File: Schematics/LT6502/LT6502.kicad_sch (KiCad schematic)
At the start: 37 parts, among them U1 TC1232, U2 W65C02S6TQG-14, U3 IS62C256AL, U4 IS62C256AL, U5 SST39SF010

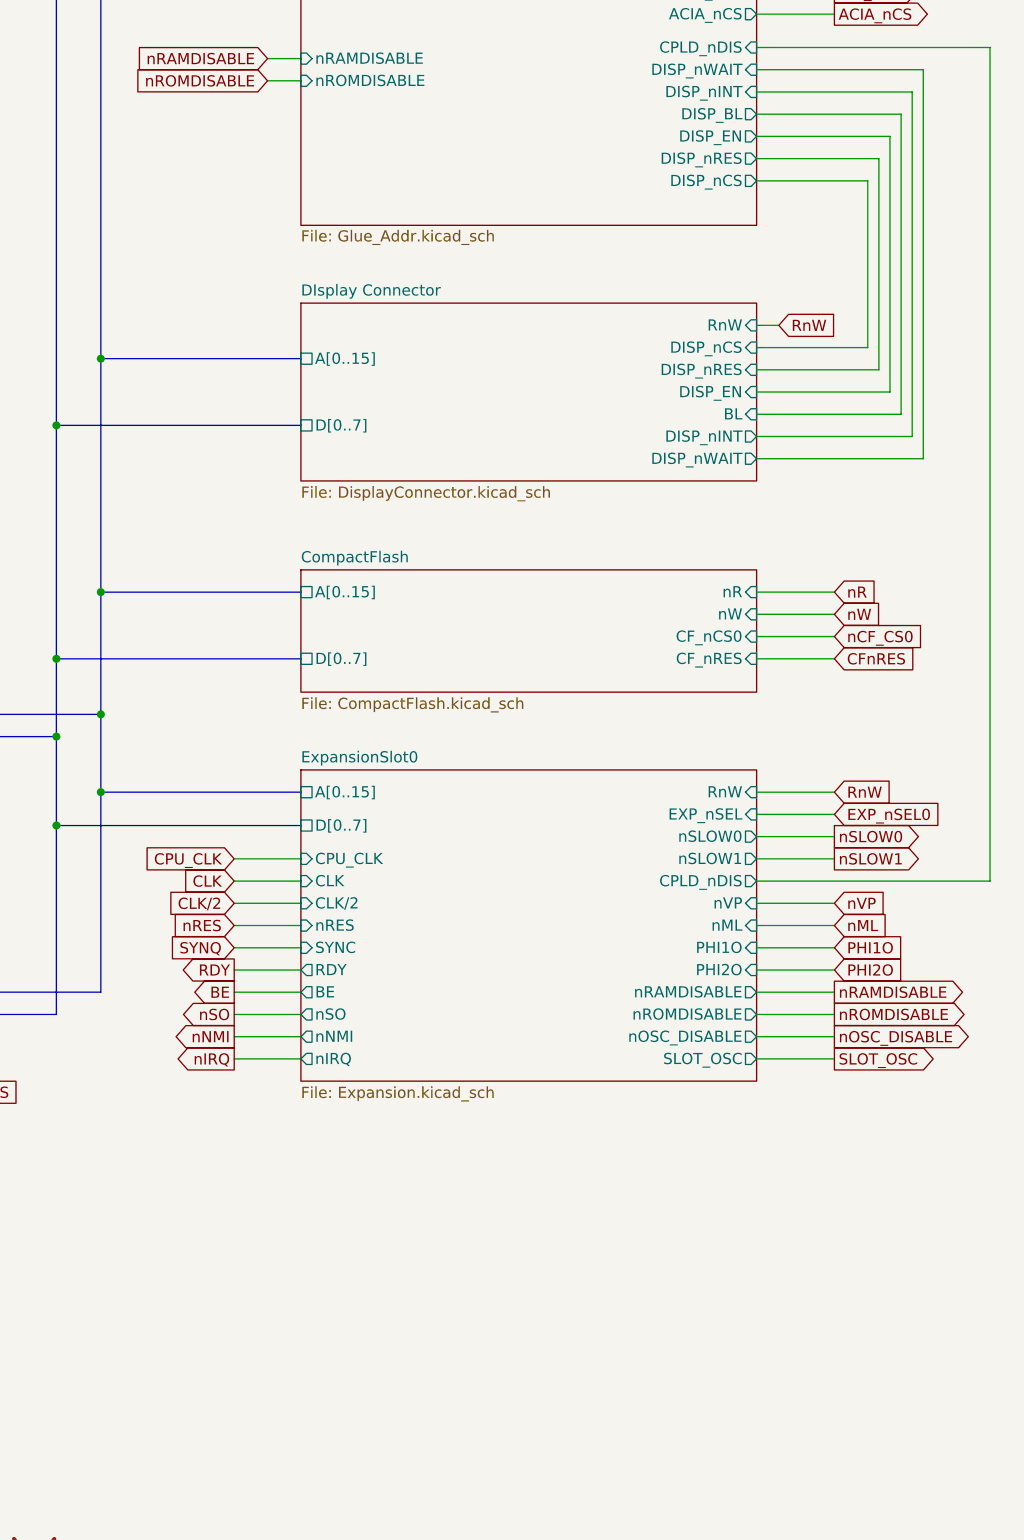
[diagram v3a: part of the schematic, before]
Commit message: Added speaker
Added a simple LM386/speaker and link to CPLD for simple audio.
Updated step files
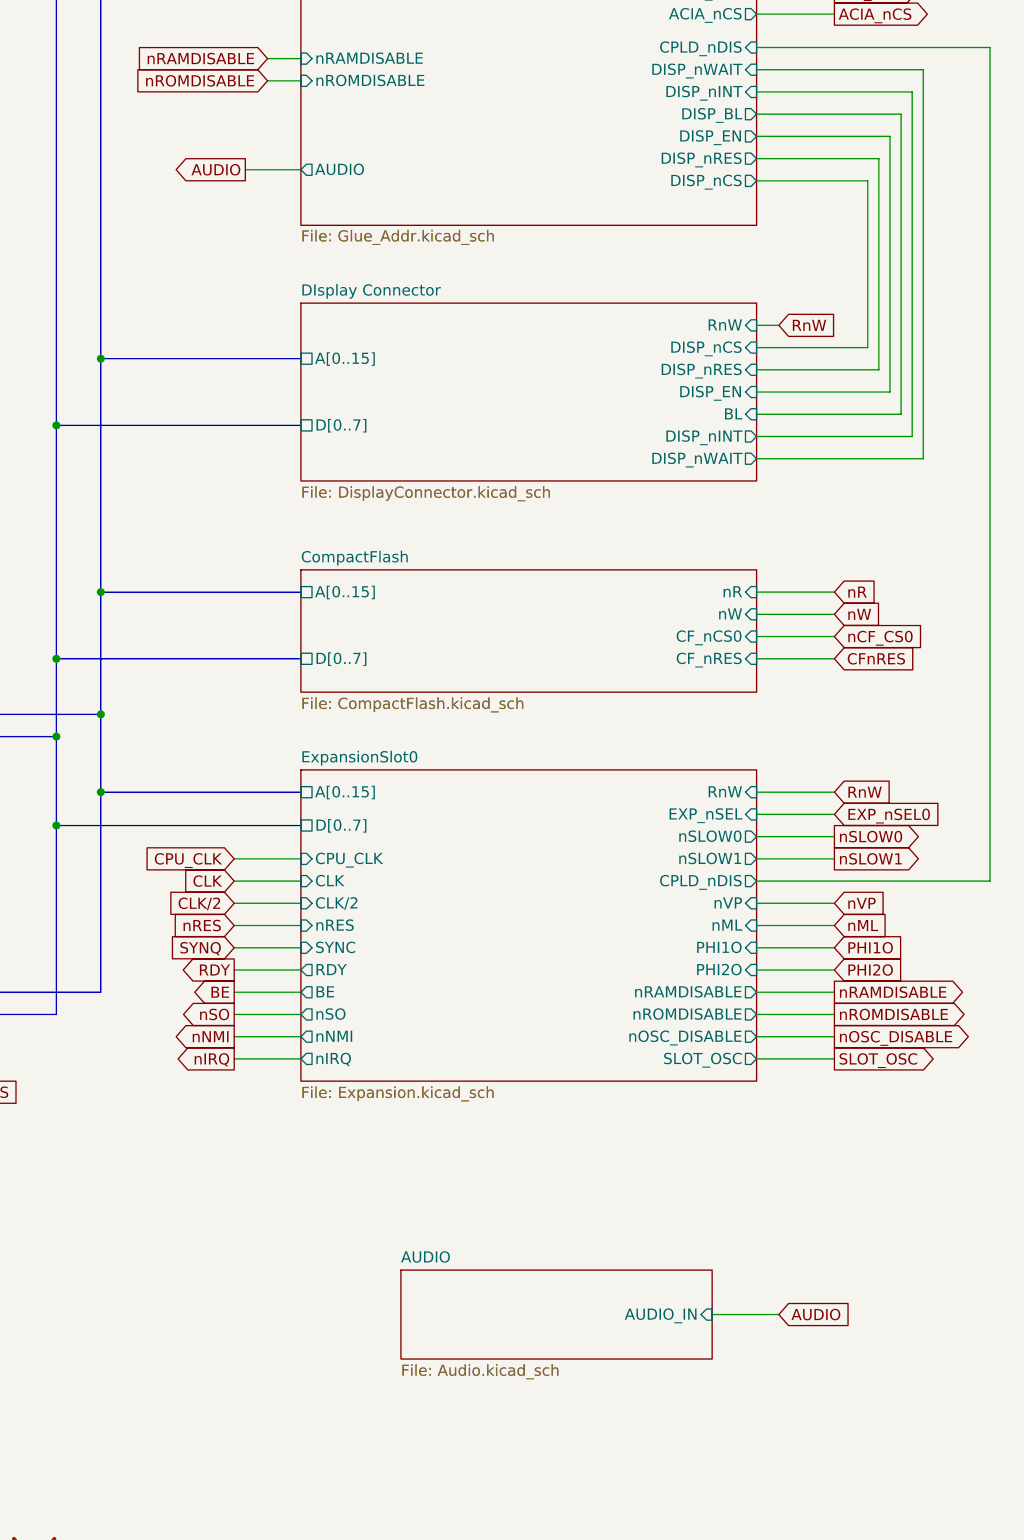
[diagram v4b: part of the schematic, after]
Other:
- added sheet AUDIO (Audio.kicad_sch)
- sheet Glue_Addr ports: added AUDIO; removed none
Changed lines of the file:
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@@
 	(wire
 		(pts
+			(xy 237.49 238.76) (xy 245.11 238.76)
+		)
+		(stroke
+			(width 0)
+			(type default)
+		)
+	)
+	(wire
+		(pts
 			(xy 92.71 44.45) (xy 92.71 41.91)
 		)
@@
 	(wire
 		(pts
+			(xy 184.15 107.95) (xy 190.5 107.95)
+		)
+		(stroke
+			(width 0)
+			(type default)
+		)
+	)
+	(wire
+		(pts
 			(xy 316.23 50.8) (xy 306.07 50.8)
 		)
@@
 		)
 	)
+	(global_label "AUDIO"
+		(shape output)
+		(at 184.15 107.95 180)
+		(fields_autoplaced yes)
+		(effects
+			(font
+				(size 1.27 1.27)
+			)
+			(justify right)
+		)
+		(property "Intersheetrefs" "${INTERSHEET_REFS}"
+			(at 175.5404 107.95 0)
+			(effects
+				(font
+					(size 1.27 1.27)
+				)
+				(justify right)
+				(hide yes)
+			)
+		)
+	)
 	(global_label "nSO"
 		(shape input)
@@
 		)
 	)
+	(global_label "AUDIO"
+		(shape input)
+		(at 245.11 238.76 0)
+		(fields_autoplaced yes)
+		(effects
+			(font
+				(size 1.27 1.27)
+			)
+			(justify left)
+		)
+		(property "Intersheetrefs" "${INTERSHEET_REFS}"
+			(at 253.7196 238.76 0)
+			(effects
+				(font
+					(size 1.27 1.27)
+				)
+				(justify left)
+				(hide yes)
+			)
+		)
+	)
 	(global_label "BE"
 		(shape input)
@@
 	)
 	(sheet
+		(at 201.93 233.68)
+		(size 35.56 10.16)
+		(exclude_from_sim no)
+		(in_bom yes)
+		(on_board yes)
+		(dnp no)
+		(fields_autoplaced yes)
+		(stroke
+			(width 0.1524)
+			(type solid)
+		)
+		(fill
+			(color 0 0 0 0.0000)
+		)
+		(property "Sheetname" "AUDIO"
+			(at 201.93 232.9684 0)
+			(effects
+				(font
+					(size 1.27 1.27)
+				)
+				(justify left bottom)
+			)
+		)
+		(property "Sheetfile" "Audio.kicad_sch"
+			(at 201.93 244.4246 0)
+			(effects
+				(font
+					(size 1.27 1.27)
+				)
+				(justify left top)
+			)
+		)
+		(pin "AUDIO_IN" input
+			(at 237.49 238.76 0)
+			(effects
+				(font
+					(size 1.27 1.27)
+				)
+				(justify right)
+			)
+		)
+		(instances
+			(project "LT6502"
+				(path "/a2243a34-697c-4939-97f7-df548e421864"
+					(page "10")
+				)
+			)
+		)
+	)
+	(sheet
 		(at 378.46 191.77)
 		(size 20.32 40.64)
@@
 			)
 		)
+		(pin "AUDIO" output
+			(at 190.5 107.95 180)
+			(effects
+				(font
+					(size 1.27 1.27)
+				)
+				(justify left)
+			)
+		)

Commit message: Updated BoMs ordered PCBs
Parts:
- C1, C2, C3, C4, C5, C53: LCSC C49678 -> C113803
- JP1, JP2, U1, U2, U3, U4: LCSC (none) -> DNF; now not fitted
- R1, R10, R7, R8: LCSC DNF -> C25890
- R9: LCSC C23179 -> C11702
- S2, U5: now not fitted
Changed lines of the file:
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@@
 			)
 		)
-		(property "LCSC" "DNF"
+		(property "LCSC" "C25890"
 			(at 33.02 162.56 0)
 			(effects
@@
 		(in_bom yes)
 		(on_board yes)
-		(dnp no)
+		(dnp yes)
 		(fields_autoplaced yes)
 		(property "Reference" "U3"
@@
 			)
 		)
+		(property "LCSC" "DNF"
+			(at 328.93 58.42 0)
+			(effects
+				(font
+					(size 1.27 1.27)
+				)
+				(hide yes)
+			)
+		)
 		(pin "7"
 		)
@@
 		(in_bom no)
 		(on_board yes)
-		(dnp no)
+		(dnp yes)
 		(fields_autoplaced yes)
 		(property "Reference" "JP1"
@@
 			)
 		)
+		(property "LCSC" "DNF"
+			(at 41.91 147.32 0)
+			(effects
+				(font
+					(size 1.27 1.27)
+				)
+				(hide yes)
+			)
+		)
 		(pin "3"
 		)
@@
 		(in_bom yes)
 		(on_board yes)
-		(dnp no)
+		(dnp yes)
 		(fields_autoplaced yes)
 		(property "Reference" "U2"
@@
 			)
 		)
+		(property "LCSC" "DNF"
+			(at 121.92 90.17 0)
+			(effects
+				(font
+					(size 1.27 1.27)
+				)
+				(hide yes)
+			)
+		)
 		(pin "2"
 		)
@@
 			)
 		)
-		(property "LCSC" "C23179"
+		(property "LCSC" "C11702"
 			(at 77.47 194.31 90)
 			(effects
@@
 			)
 		)
-		(property "LCSC" "C49678"
+		(property "LCSC" "C113803"
 			(at 54.61 265.43 0)
 			(effects
@@
 			)
 		)
-		(property "LCSC" "DNF"
+		(property "LCSC" "C25890"
 			(at 92.71 38.1 0)
 			(effects
@@
 			)
 		)
-		(property "LCSC" "C49678"
+		(property "LCSC" "C113803"
 			(at 31.75 265.43 0)
 			(effects
@@
 			)
 		)
-		(property "LCSC" "C49678"
+		(property "LCSC" "C113803"
 			(at 88.9 265.43 0)
 			(effects
@@
 		(in_bom no)
 		(on_board yes)
-		(dnp no)
+		(dnp yes)
 		(property "Reference" "JP2"
 			(at 60.96 134.62 0)
@@
 			)
 		)
+		(property "LCSC" "DNF"
+			(at 60.96 140.97 0)
+			(effects
+				(font
+					(size 1.27 1.27)
+				)
+				(hide yes)
+			)
+		)
 		(pin "3"
 		)
@@
 			)
 		)
-		(property "LCSC" "C49678"
+		(property "LCSC" "C113803"
 			(at 25.4 265.43 0)
 			(effects
@@
 		(in_bom yes)
 		(on_board yes)
-		(dnp no)
+		(dnp yes)
 		(fields_autoplaced yes)
 		(property "Reference" "U4"
@@
 			)
 		)
+		(property "LCSC" "DNF"
+			(at 328.93 119.38 0)
+			(effects
+				(font
+					(size 1.27 1.27)
+				)
+				(hide yes)
+			)
+		)
 		(pin "7"
 		)
@@
 		(in_bom yes)
 		(on_board yes)
-		(dnp no)
+		(dnp yes)
 		(property "Reference" "S2"
 			(at 27.178 183.134 0)
@@
 		(in_bom yes)
 		(on_board yes)
-		(dnp no)
+		(dnp yes)
 		(property "Reference" "U5"
 			(at 337.185 158.75 0)
@@
 			)
 		)
-		(property "LCSC" "DNF"
+		(property "LCSC" "C25890"
 			(at 83.82 38.1 0)
 			(effects
@@
 			)
 		)
-		(property "LCSC" "C49678"
+		(property "LCSC" "C113803"
 			(at 60.96 265.43 0)
 			(effects
@@
 		(in_bom yes)
 		(on_board yes)
-		(dnp no)
+		(dnp yes)
 		(fields_autoplaced yes)
 		(property "Reference" "U1"
@@
 			)
 		)
+		(property "LCSC" "DNF"
+			(at 74.93 167.64 0)
+			(effects
+				(font
+					(size 1.27 1.27)
+				)
+				(hide yes)
+			)
+		)
 		(pin "2"
 		)
@@
 			)
 		)
-		(property "LCSC" "DNF"
+		(property "LCSC" "C25890"
 			(at 99.06 160.02 0)
 			(effects
@@
 			)
 		)
-		(property "LCSC" "C49678"
+		(property "LCSC" "C113803"
 			(at 82.55 265.43 0)
 			(effects

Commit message: Auto stash before merge of "main" and "origin/main"
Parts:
- added TP7: TestPoint, TestPoint:TestPoint_Loop_D1.80mm_Drill1.0mm_Beaded, symbol Connector:TestPoint
- S2, U1, U2, U3, U4, U5: now fitted
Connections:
- net at R1.2, S2.1, S2.2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: now also TP7.1
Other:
- sheet DIsplay Connector renamed Display Connector
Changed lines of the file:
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@@
 		)
 	)
+	(text_box "V1.0-V1.1 Changes\nAdded cutout for reset switch\nAdded cutout for LS1 and moved it\nExpanded pads on L2 for ease of soldering\nChange R46 to 51K\nChange R47 to 120K\nAdded Pull ups to SLOW0 and SLOW1"
+		(exclude_from_sim no)
+		(at 179.07 238.76 0)
+		(size 100.33 38.1)
+		(margins 0.9525 0.9525 0.9525 0.9525)
+		(stroke
+			(width 0)
+			(type solid)
+		)
+		(fill
+			(type none)
+		)
+		(effects
+			(font
+				(size 1.27 1.27)
+			)
+			(justify left top)
+		)
+	)
 	(junction
 		(at 83.82 46.99)
@@
 	)
 	(junction
+		(at 52.07 181.61)
+		(diameter 0)
+		(color 0 0 0 0)
+	)
+	(junction
 		(at 162.56 49.53)
 		(diameter 0)
@@
 	(wire
 		(pts
-			(xy 237.49 238.76) (xy 245.11 238.76)
+			(xy 233.68 226.06) (xy 241.3 226.06)
 		)
 		(stroke
@@
 		)
 	)
+	(wire
+		(pts
+			(xy 62.23 180.34) (xy 62.23 181.61)
+		)
+		(stroke
+			(width 0)
+			(type default)
+		)
+	)
 	(bus
 		(pts
@@
 	(wire
 		(pts
+			(xy 62.23 181.61) (xy 52.07 181.61)
+		)
+		(stroke
+			(width 0)
+			(type default)
+		)
+	)
+	(wire
+		(pts
 			(xy 257.81 104.14) (xy 257.81 133.35)
 		)
@@
 	(global_label "AUDIO"
 		(shape input)
-		(at 245.11 238.76 0)
+		(at 241.3 226.06 0)
 		(fields_autoplaced yes)
 		(effects
@@
 		)
 		(property "Intersheetrefs" "${INTERSHEET_REFS}"
-			(at 253.7196 238.76 0)
+			(at 249.9096 226.06 0)
 			(effects
 				(font
@@
 		(in_bom yes)
 		(on_board yes)
-		(dnp yes)
+		(dnp no)
 		(fields_autoplaced yes)
 		(property "Reference" "U3"
@@
 		(in_bom yes)
 		(on_board yes)
-		(dnp yes)
+		(dnp no)
 		(fields_autoplaced yes)
 		(property "Reference" "U2"
@@
 	)
 	(symbol
+		(lib_id "Connector:TestPoint")
+		(at 62.23 180.34 0)
+		(unit 1)
+		(exclude_from_sim no)
+		(in_bom no)
+		(on_board yes)
+		(dnp yes)
+		(property "Reference" "TP7"
+			(at 60.96 174.752 0)
+			(effects
+				(font
+					(size 1.27 1.27)
+				)
+				(justify left)
+			)
+		)
+		(property "Value" "TestPoint"
+			(at 64.77 178.3079 0)
+			(effects
+				(font
+					(size 1.27 1.27)
+				)
+				(justify left)
+				(hide yes)
+			)
+		)
+		(property "Footprint" "TestPoint:TestPoint_Loop_D1.80mm_Drill1.0mm_Beaded"
+			(at 67.31 180.34 0)
+			(effects
+				(font
+					(size 1.27 1.27)
+				)
+				(hide yes)
+			)
+		)
+		(property "Datasheet" "~"
+			(at 67.31 180.34 0)
+			(effects
+				(font
+					(size 1.27 1.27)
+				)
+				(hide yes)
+			)
+		)
+		(property "Description" "test point"
+			(at 62.23 180.34 0)
+			(effects
+				(font
+					(size 1.27 1.27)
+				)
+				(hide yes)
+			)
+		)
+		(property "LCSC" "DNF"
+			(at 62.23 180.34 0)
+			(effects
+				(font
+					(size 1.27 1.27)
+				)
+				(hide yes)
+			)
+		)
+		(pin "1"
+		)
+		(instances
+			(project "LT6502"
+				(path "/a2243a34-697c-4939-97f7-df548e421864"
+					(reference "TP7")
+					(unit 1)
+				)
+			)
+		)
+	)
+	(symbol
 		(lib_id "power:GND")
 		(at 69.85 140.97 0)
@@
 		(in_bom yes)
 		(on_board yes)
-		(dnp yes)
+		(dnp no)
 		(fields_autoplaced yes)
 		(property "Reference" "U4"
@@
 		(in_bom yes)
 		(on_board yes)
-		(dnp yes)
+		(dnp no)
 		(property "Reference" "S2"
 			(at 27.178 183.134 0)
@@
 		(in_bom yes)
 		(on_board yes)
-		(dnp yes)
+		(dnp no)
 		(property "Reference" "U5"
 			(at 337.185 158.75 0)
@@
 		(in_bom yes)
 		(on_board yes)
-		(dnp yes)
+		(dnp no)
 		(fields_autoplaced yes)
 		(property "Reference" "U1"
@@
 	)
 	(sheet
-		(at 201.93 233.68)
+		(at 198.12 220.98)
 		(size 35.56 10.16)
 		(exclude_from_sim no)
@@
 		)
 		(property "Sheetname" "AUDIO"
-			(at 201.93 232.9684 0)
+			(at 198.12 220.2684 0)
 			(effects
 				(font
@@
 		)
 		(property "Sheetfile" "Audio.kicad_sch"
-			(at 201.93 244.4246 0)
+			(at 198.12 231.7246 0)
 			(effects
 				(font
@@
 		)
 		(pin "AUDIO_IN" input
-			(at 237.49 238.76 0)
+			(at 233.68 226.06 0)
 			(effects
 				(font
@@
 			(color 0 0 0 0.0000)
 		)
-		(property "Sheetname" "DIsplay Connector"
+		(property "Sheetname" "Display Connector"
 			(at 190.5 122.4784 0)
 			(effects
